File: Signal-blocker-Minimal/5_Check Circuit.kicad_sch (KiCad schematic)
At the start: 7 parts

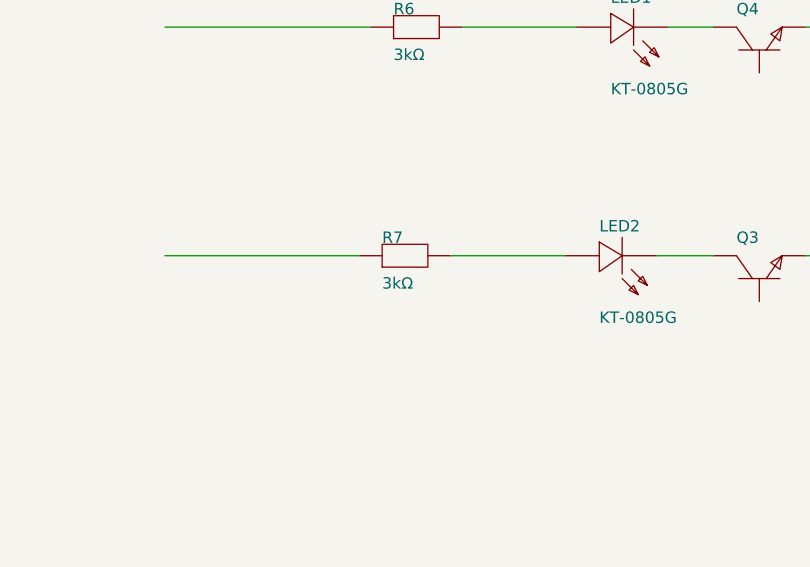
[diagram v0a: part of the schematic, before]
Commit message: Version 2.1 Update！
Fix some circuit!
More stabler!
Replace all the restrictor and capacitor into 0603 packaging!
create BOM excel,Bill of Material.
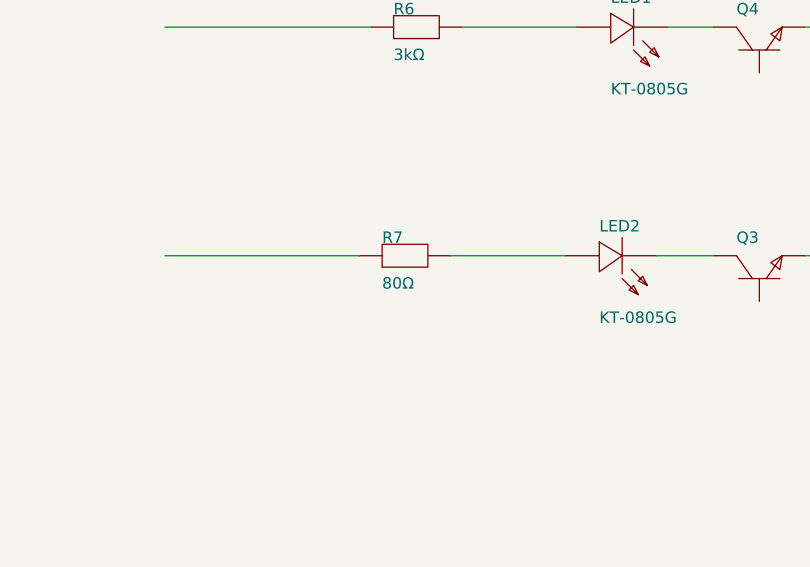
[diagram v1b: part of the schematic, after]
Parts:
- removed ?: (no value), ProPrj_Sig-easyedapro:, symbol ProPrj_Sig-easyedapro:Drawing-Symbol_A4
- removed LED1, LED2: KT-0805G, ProPrj_Sig-easyedapro:LED0805-R-RD, symbol ProPrj_Sig-easyedapro:0805G (Green)
- removed Q3, Q4: (no value), ProPrj_Sig-easyedapro:S8050_SOT-23, symbol ProPrj_Sig-easyedapro:NPN
- removed R6, R7: 3kΩ, ProPrj_Sig-easyedapro:R2010, symbol ProPrj_Sig-easyedapro:RS-10K3001FT
- added ?: (no value), Signal-blo-easyedapro:, symbol Signal-blo-easyedapro:Drawing-Symbol_A4
- added LED1, LED2: KT-0805G, Signal-blo-easyedapro:LED0805-R-RD, symbol Signal-blo-easyedapro:0805G (Green)
- added Q3, Q4: (no value), Signal-blo-easyedapro:S8050_SOT-23, symbol Signal-blo-easyedapro:NPN
- added R6: 3kΩ, Signal-blo-easyedapro:R2010, symbol Signal-blo-easyedapro:RS-10K3001FT
- added R7: 80Ω, Signal-blo-easyedapro:R2010, symbol Signal-blo-easyedapro:RS-10K3001FT
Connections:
- net GND: now also Q3.2, Q4.2
- new net: LED2.1 (A), R7.2
- new net: LED2.2 (K), Q3.3
- new net: LED1.1 (A), R6.2
- new net: LED1.2 (K), Q4.3
